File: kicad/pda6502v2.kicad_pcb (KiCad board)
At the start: 2 copper layers, 4 parts, among them U1 W65C02SxP, U2 AS6C62256-55PCN, U3 W65C22SxP, U4 AS6C62256-55PCN

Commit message: Lots of progress on schematic, some PCB part placement.
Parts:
- added C1: 0.1μF, Capacitor_SMD:C_0805_2012Metric_Pad1.18x1.45mm_HandSolder, B.Cu at (129.5, 91.4)
- added C10: 0.1μF, Capacitor_SMD:C_0805_2012Metric_Pad1.18x1.45mm_HandSolder, B.Cu at (119.4, 108.0)
- added C11: 0.1μF, Capacitor_SMD:C_0805_2012Metric_Pad1.18x1.45mm_HandSolder, B.Cu at (125.7, 133.9)
- added C12: 100uF, Capacitor_THT:CP_Radial_D5.0mm_P2.00mm, F.Cu at (106.7, 59.7)
- added C13: 10uF, Capacitor_THT:CP_Radial_D5.0mm_P2.00mm, F.Cu at (106.7, 67.7)
- added C14: 0.1μF, Capacitor_SMD:C_0805_2012Metric_Pad1.18x1.45mm_HandSolder, B.Cu at (125.7, 128.8)
- added C15: 0.1μF, Capacitor_SMD:C_0805_2012Metric_Pad1.18x1.45mm_HandSolder, B.Cu at (125.7, 123.7)
- added C16: 0.1μF, Capacitor_SMD:C_0805_2012Metric_Pad1.18x1.45mm_HandSolder, B.Cu at (125.7, 118.7)
- added C17: 0.1μF, Capacitor_SMD:C_0805_2012Metric_Pad1.18x1.45mm_HandSolder, B.Cu at (130.7, 133.9)
- added C18: 10nF, Capacitor_SMD:C_0805_2012Metric_Pad1.18x1.45mm_HandSolder, B.Cu at (119.4, 86.4)
- added C19: 10nF, Capacitor_SMD:C_0805_2012Metric_Pad1.18x1.45mm_HandSolder, B.Cu at (119.4, 82.5)
- added C2: 0.1μF, Capacitor_SMD:C_0805_2012Metric_Pad1.18x1.45mm_HandSolder, B.Cu at (170.2, 91.4)
- added C20: 10uF, Capacitor_SMD:C_0805_2012Metric_Pad1.18x1.45mm_HandSolder, B.Cu at (114.3, 86.4)
- added C21: 10uF, Capacitor_SMD:C_0805_2012Metric_Pad1.18x1.45mm_HandSolder, B.Cu at (114.3, 82.5)
- added C22: 0.1μF, Capacitor_SMD:C_0805_2012Metric_Pad1.18x1.45mm_HandSolder, B.Cu at (130.7, 128.8)
- added C23: 0.1μF, Capacitor_SMD:C_0805_2012Metric_Pad1.18x1.45mm_HandSolder, B.Cu at (130.7, 123.7)
- added C24: 0.1μF, Capacitor_SMD:C_0805_2012Metric_Pad1.18x1.45mm_HandSolder, B.Cu at (130.7, 118.7)
- added C3: 0.1μF, Capacitor_SMD:C_0805_2012Metric_Pad1.18x1.45mm_HandSolder, B.Cu at (169.9, 116.6)
- added C4: 0.1μF, Capacitor_SMD:C_0805_2012Metric_Pad1.18x1.45mm_HandSolder, B.Cu at (149.9, 124.5)
- added C5: 0.1μF, Capacitor_SMD:C_0805_2012Metric_Pad1.18x1.45mm_HandSolder, B.Cu at (185.4, 50.8)
- added C6: 0.1μF, Capacitor_SMD:C_0805_2012Metric_Pad1.18x1.45mm_HandSolder, B.Cu at (185.4, 71.1)
- added C7: 0.1μF, Capacitor_SMD:C_0805_2012Metric_Pad1.18x1.45mm_HandSolder, B.Cu at (185.4, 66.0)
- added C8: 0.1μF, Capacitor_SMD:C_0805_2012Metric_Pad1.18x1.45mm_HandSolder, B.Cu at (185.4, 86.4)
- added C9: 0.1μF, Capacitor_SMD:C_0805_2012Metric_Pad1.18x1.45mm_HandSolder, B.Cu at (149.9, 81.3)
- added D1: 1N5819, Diode_THT:D_DO-41_SOD81_P10.16mm_Horizontal, F.Cu at (120.7, 50.8)
- added D10: LED, LED_SMD:LED_0805_2012Metric_Pad1.15x1.40mm_HandSolder, F.Cu at (193.0, 92.2)
- added D2: LED, LED_THT:LED_D3.0mm, F.Cu at (106.7, 76.2)
- added D3: LED, LED_SMD:LED_0805_2012Metric_Pad1.15x1.40mm_HandSolder, F.Cu at (193.0, 109.9)
- added D4: LED, LED_SMD:LED_0805_2012Metric_Pad1.15x1.40mm_HandSolder, F.Cu at (193.0, 107.4)
- added D5: LED, LED_SMD:LED_0805_2012Metric_Pad1.15x1.40mm_HandSolder, F.Cu at (193.0, 104.9)
- added D6: LED, LED_SMD:LED_0805_2012Metric_Pad1.15x1.40mm_HandSolder, F.Cu at (193.0, 102.3)
- added D7: LED, LED_SMD:LED_0805_2012Metric_Pad1.15x1.40mm_HandSolder, F.Cu at (193.0, 99.8)
- added D8: LED, LED_SMD:LED_0805_2012Metric_Pad1.15x1.40mm_HandSolder, F.Cu at (193.0, 97.2)
- added D9: LED, LED_SMD:LED_0805_2012Metric_Pad1.15x1.40mm_HandSolder, F.Cu at (193.0, 94.7)
- added J1: GPIOA, Connector_PinHeader_2.54mm:PinHeader_2x07_P2.54mm_Vertical, F.Cu at (190.5, 50.8)
- added J2: GPIOB, Connector_PinHeader_2.54mm:PinHeader_2x07_P2.54mm_Vertical, F.Cu at (190.5, 71.1)
- added J3: UART, Connector_PinHeader_2.54mm:PinHeader_2x06_P2.54mm_Vertical, F.Cu at (190.5, 116.8)
- added J4: Screw_Terminal_01x02, TerminalBlock_Phoenix:TerminalBlock_Phoenix_MPT-0,5-2-2.54_1x02_P2.54mm_Horizontal, F.Cu at (104.1, 50.8)
- added J5: Conn_01x02, Connector_PinHeader_2.54mm:PinHeader_1x02_P2.54mm_Vertical, F.Cu at (111.8, 45.7)
- added J6: PMOD A, Connector_PinSocket_2.54mm:PinSocket_2x06_P2.54mm_Horizontal, F.Cu at (109.2, 116.8)
- added J7: PMOD B, Connector_PinSocket_2.54mm:PinSocket_2x06_P2.54mm_Horizontal, F.Cu at (109.2, 94.0)
- added JP1: Jumper, Connector_PinHeader_2.54mm:PinHeader_1x02_P2.54mm_Vertical, F.Cu at (119.4, 45.7)
- added R1: 10K, Resistor_SMD:R_0805_2012Metric_Pad1.20x1.40mm_HandSolder, B.Cu at (169.9, 121.7)
- added R10: 100Ω, Resistor_SMD:R_0805_2012Metric_Pad1.20x1.40mm_HandSolder, B.Cu at (115.2, 94.3)
- added R11: 100Ω, Resistor_SMD:R_0805_2012Metric_Pad1.20x1.40mm_HandSolder, B.Cu at (120.2, 96.8)
- added R12: 100Ω, Resistor_SMD:R_0805_2012Metric_Pad1.20x1.40mm_HandSolder, B.Cu at (115.2, 96.8)
- added R13: 100Ω, Resistor_SMD:R_0805_2012Metric_Pad1.20x1.40mm_HandSolder, B.Cu at (120.2, 120.3)
- added R14: 100Ω, Resistor_SMD:R_0805_2012Metric_Pad1.20x1.40mm_HandSolder, B.Cu at (115.2, 120.3)
- added R15: 100Ω, Resistor_SMD:R_0805_2012Metric_Pad1.20x1.40mm_HandSolder, B.Cu at (120.2, 117.8)
- added R16: 100Ω, Resistor_SMD:R_0805_2012Metric_Pad1.20x1.40mm_HandSolder, B.Cu at (115.2, 117.8)
- added R17: 100Ω, Resistor_SMD:R_0805_2012Metric_Pad1.20x1.40mm_HandSolder, B.Cu at (120.2, 101.9)
- added R18: 100Ω, Resistor_SMD:R_0805_2012Metric_Pad1.20x1.40mm_HandSolder, B.Cu at (115.2, 101.9)
- added R19: 100Ω, Resistor_SMD:R_0805_2012Metric_Pad1.20x1.40mm_HandSolder, B.Cu at (120.2, 104.5)
- added R2: 10K, Resistor_SMD:R_0805_2012Metric_Pad1.20x1.40mm_HandSolder, B.Cu at (175.0, 121.7)
- added R20: 100Ω, Resistor_SMD:R_0805_2012Metric_Pad1.20x1.40mm_HandSolder, B.Cu at (115.2, 104.5)
- added R21: 10K, Resistor_SMD:R_0805_2012Metric_Pad1.20x1.40mm_HandSolder, B.Cu at (102.9, 58.4)
- added R22: 10K, Resistor_SMD:R_0805_2012Metric_Pad1.20x1.40mm_HandSolder, B.Cu at (102.9, 62.2)
- added R23: 10K, Resistor_SMD:R_0805_2012Metric_Pad1.20x1.40mm_HandSolder, B.Cu at (128.2, 113.6)
- added R24: ?, Resistor_SMD:R_0805_2012Metric_Pad1.20x1.40mm_HandSolder, B.Cu at (102.9, 66.0)
- added R25: ?, Resistor_SMD:R_0805_2012Metric_Pad1.20x1.40mm_HandSolder, B.Cu at (102.9, 69.8)
- added R26: ?, Resistor_SMD:R_0805_2012Metric_Pad1.20x1.40mm_HandSolder, B.Cu at (102.9, 73.7)
- added R27: ?, Resistor_SMD:R_0805_2012Metric_Pad1.20x1.40mm_HandSolder, B.Cu at (102.9, 77.5)
- added R28: 1K, Resistor_SMD:R_0805_2012Metric_Pad1.20x1.40mm_HandSolder, B.Cu at (108.0, 72.4)
- added R29: 1K, Resistor_SMD:R_0805_2012Metric_Pad1.20x1.40mm_HandSolder, B.Cu at (187.9, 109.9)
- added R3: 10K, Resistor_SMD:R_0805_2012Metric_Pad1.20x1.40mm_HandSolder, B.Cu at (169.9, 124.2)
- added R30: 1K, Resistor_SMD:R_0805_2012Metric_Pad1.20x1.40mm_HandSolder, B.Cu at (187.9, 107.4)
- added R31: 1K, Resistor_SMD:R_0805_2012Metric_Pad1.20x1.40mm_HandSolder, B.Cu at (187.9, 104.9)
- added R32: 1K, Resistor_SMD:R_0805_2012Metric_Pad1.20x1.40mm_HandSolder, B.Cu at (187.9, 102.3)
- added R33: 1K, Resistor_SMD:R_0805_2012Metric_Pad1.20x1.40mm_HandSolder, B.Cu at (187.9, 99.8)
- added R34: 1K, Resistor_SMD:R_0805_2012Metric_Pad1.20x1.40mm_HandSolder, B.Cu at (187.9, 97.2)
- added R35: 1K, Resistor_SMD:R_0805_2012Metric_Pad1.20x1.40mm_HandSolder, B.Cu at (187.9, 94.7)
- added R36: 1K, Resistor_SMD:R_0805_2012Metric_Pad1.20x1.40mm_HandSolder, B.Cu at (187.9, 92.2)
- added R4: 10K, Resistor_SMD:R_0805_2012Metric_Pad1.20x1.40mm_HandSolder, B.Cu at (175.0, 124.2)
- added R5: 100Ω, Resistor_SMD:R_0805_2012Metric_Pad1.20x1.40mm_HandSolder, B.Cu at (120.2, 128.0)
- added R6: 100Ω, Resistor_SMD:R_0805_2012Metric_Pad1.20x1.40mm_HandSolder, B.Cu at (115.2, 128.0)
- added R7: 100Ω, Resistor_SMD:R_0805_2012Metric_Pad1.20x1.40mm_HandSolder, B.Cu at (120.2, 125.4)
- added R8: 100Ω, Resistor_SMD:R_0805_2012Metric_Pad1.20x1.40mm_HandSolder, B.Cu at (115.2, 125.4)
- added R9: 100Ω, Resistor_SMD:R_0805_2012Metric_Pad1.20x1.40mm_HandSolder, B.Cu at (120.2, 94.3)
- added REF**: MountingHole_3.2mm_M3, MountingHole:MountingHole_3.2mm_M3, F.Cu at (193.7, 136.3)
- added REF**: MountingHole_3.2mm_M3, MountingHole:MountingHole_3.2mm_M3, F.Cu at (101.7, 136.3)
- added REF**: MountingHole_3.2mm_M3, MountingHole:MountingHole_3.2mm_M3, F.Cu at (193.7, 44.3)
- added REF**: MountingHole_3.2mm_M3, MountingHole:MountingHole_3.2mm_M3, F.Cu at (101.7, 44.3)
- added SW1: SW_Push, Button_Switch_THT:SW_Tactile_Straight_KSA0Axx1LFTR, F.Cu at (101.6, 88.9)
- added U10: LT3030, Package_SO:HTSSOP-20-1EP_4.4x6.5mm_P0.65mm_EP2.85x4mm, F.Cu at (116.8, 83.8)
- added U5: AS6C4002-55PCN, Package_DIP:DIP-32_W15.24mm, F.Cu at (144.8, 88.9)
- added U6: AS6C4008-55PCN, Package_DIP:DIP-32_W15.24mm, F.Cu at (144.8, 45.7)
- added U7: AT25M01, Package_SO:SOIC-8_3.9x4.9mm_P1.27mm, F.Cu at (118.1, 102.9)
- added U8: ICE40HX4K-TQ144, Package_QFP:TQFP-144_20x20mm_P0.5mm, F.Cu at (127.0, 123.2)
- added U9: LM1117-3.3, Package_TO_SOT_THT:TO-220-3_Horizontal_TabDown, F.Cu at (114.3, 76.2)
- added X1: 3.6864 MHz, Oscillator:Oscillator_DIP-8, F.Cu at (168.9, 108.0)
- added X2: 10 MHz, Oscillator:Oscillator_DIP-8, F.Cu at (128.3, 106.7)
- U2: value AS6C62256-55PCN -> W65C22SxP; footprint Package_DIP:DIP-28_W15.24mm -> Package_DIP:DIP-40_W15.24mm
- U3: value W65C22SxP -> SC28L92A1B; footprint Package_DIP:DIP-40_W15.24mm -> Package_QFP:PQFP-44_10x10mm_P0.8mm
- U4: value AS6C62256-55PCN -> DS1818; footprint Package_DIP:DIP-28_W15.24mm -> Package_TO_SOT_SMD:SOT-23_Handsoldering
- moved U3 103.7 mm to (172.7, 120.4)
- moved U2 99.1 mm to (165.1, 45.7)
- moved U1 68.3 mm to (124.5, 45.7)
- moved U4 16.6 mm to (118.1, 94.0), turned to 180 degrees
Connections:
- U1 pad 1: Net-(U1-Pad1) -> /~VECPULL
- U1 pad 10: /ADDR1 -> /A1
- U1 pad 11: /ADDR2 -> /A2
- U1 pad 12: /ADDR3 -> /A3
- U1 pad 13: /ADDR4 -> /A4
- U1 pad 14: /ADDR5 -> /A5
- U1 pad 15: /ADDR6 -> /A6
- U1 pad 16: /ADDR7 -> /A7
- U1 pad 17: /ADDR8 -> /A8
- U1 pad 18: /ADDR9 -> /A9
- U1 pad 19: /ADDR10 -> /A10
- U1 pad 2: Net-(U1-Pad2) -> /READY
- U1 pad 20: /ADDR11 -> /A11
- U1 pad 22: /ADDR12 -> /A12
- U1 pad 23: /ADDR13 -> /A13
- U1 pad 24: /ADDR14 -> /A14
- U1 pad 25: /ADDR15 -> /A15
- U1 pad 26: /DATA7 -> /D7
- U1 pad 27: /DATA6 -> /D6
- U1 pad 28: /DATA5 -> /D5
- U1 pad 29: /DATA4 -> /D4
- U1 pad 30: /DATA3 -> /D3
- U1 pad 31: /DATA2 -> /D2
- U1 pad 32: /DATA1 -> /D1
- U1 pad 33: /DATA0 -> /D0
- U1 pad 34: Net-(U1-Pad34) -> /R~W
- U1 pad 36: Net-(U1-Pad36) -> /BUSEN
- U1 pad 37: /CLK -> /CLOCK
- U1 pad 38: Net-(U1-Pad38) -> /~SETOV
- U1 pad 4: Net-(U1-Pad4) -> /~IRQ
- U1 pad 40: /RESET -> /~RESET
- U1 pad 5: Net-(U1-Pad5) -> /~MLOCK
- U1 pad 6: Net-(U1-Pad6) -> /~NMIRQ
- U1 pad 7: Net-(U1-Pad7) -> /SYNC
- U1 pad 9: /ADDR0 -> /A0
- U2 pad 1: /ADDR14 -> GND
- U2 pad 10: /ADDR0 -> /PORTB_0
- U2 pad 11: /DATA0 -> /PORTB_1
- U2 pad 12: /DATA1 -> /PORTB_2
- U2 pad 13: /DATA2 -> /PORTB_3
- U2 pad 14: GND -> /PORTB_4
- U2 pad 15: /DATA3 -> /PORTB_5
- U2 pad 16: /DATA4 -> /PORTB_6
- U2 pad 17: /DATA5 -> /PORTB_7
- U2 pad 18: /DATA6 -> /PORTB_C1
- U2 pad 19: /DATA7 -> /PORTB_C2
- U2 pad 2: /ADDR12 -> /PORTA_0
- U2 pad 20: /RAM_LO_~CS -> +3V3
- U2 pad 21: /ADDR10 -> /VIA_~IRQ
- U2 pad 22: /RAM_LO_~CS -> /R~W
- U2 pad 23: /ADDR11 -> /VIA_~CS
- U2 pad 24: /ADDR9 -> +3V3
- U2 pad 25: /ADDR8 -> /CLOCK
- U2 pad 26: /ADDR13 -> /D7
- U2 pad 27: /RWB -> /D6
- U2 pad 28: +3V3 -> /D5
- U2 pad 3: /ADDR7 -> /PORTA_1
- U2 pad 4: /ADDR6 -> /PORTA_2
- U2 pad 5: /ADDR5 -> /PORTA_3
- U2 pad 6: /ADDR4 -> /PORTA_4
- U2 pad 7: /ADDR3 -> /PORTA_5
- U2 pad 8: /ADDR2 -> /PORTA_6
- U2 pad 9: /ADDR1 -> /PORTA_7
- U3 pad 1: GND -> /A3
- U3 pad 10: Net-(U3-Pad10) -> /UART_TXB~IRQ
- U3 pad 11: Net-(U3-Pad11) -> /UART_IM
- U3 pad 12: Net-(U3-Pad12) -> /D1
- U3 pad 13: Net-(U3-Pad13) -> /D3
- U3 pad 14: Net-(U3-Pad14) -> /D5
- U3 pad 15: Net-(U3-Pad15) -> /D7
- U3 pad 16: Net-(U3-Pad16) -> GND
- U3 pad 17: Net-(U3-Pad17) -> GND
- U3 pad 18: Net-(U3-Pad18) -> /UART_~IRQ
- U3 pad 19: Net-(U3-Pad19) -> /D6
- U3 pad 2: Net-(U3-Pad2) -> /UARTA_CTS
- U3 pad 20: +3V3 -> /D4
- U3 pad 21: Net-(U3-Pad21) -> /D2
- U3 pad 22: Net-(U3-Pad22) -> /D0
- U3 pad 24: Net-(U3-Pad24) -> /UART_TXA~IRQ
- U3 pad 25: /CLK -> /UART_RXA~IRQ
- U3 pad 26: /DATA7 -> Net-(U3-Pad26)
- U3 pad 27: /DATA6 -> /UARTA_RTS
- U3 pad 28: /DATA5 -> /UARTA_TX
- U3 pad 29: /DATA4 -> /UARTA_RX
- U3 pad 3: Net-(U3-Pad3) -> /UART_~WRN
- U3 pad 30: /DATA3 -> Net-(U3-Pad30)
- U3 pad 31: /DATA2 -> Net-(U3-Pad31)
- U3 pad 32: /DATA1 -> /RESET
- U3 pad 33: /DATA0 -> /UART_~CS
- U3 pad 35: /ADDR3 -> Net-(U3-Pad35)
- U3 pad 36: /ADDR2 -> Net-(U3-Pad36)
- U3 pad 37: /ADDR1 -> Net-(U3-Pad37)
- U3 pad 38: /ADDR0 -> +3V3
- U3 pad 39: Net-(U3-Pad39) -> +3V3
- U3 pad 4: Net-(U3-Pad4) -> /UART_~RDN
- U3 pad 40: Net-(U3-Pad40) -> /A0
- U3 pad 5: Net-(U3-Pad5) -> /UARTB_RX
- U3 pad 6: Net-(U3-Pad6) -> /UARTB_TX
- U3 pad 7: Net-(U3-Pad7) -> /UARTB_RTS
- U3 pad 9: Net-(U3-Pad9) -> /UART_RXB~IRQ
- U4 pad 1: /ADDR14 -> /~RESET
- U4 pad 2: /ADDR12 -> +3V3
- U4 pad 3: /ADDR7 -> GND
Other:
- board outline added: 100 x 100 mm
- copper layers 2 -> 4
- board text added: "pda6502v2"

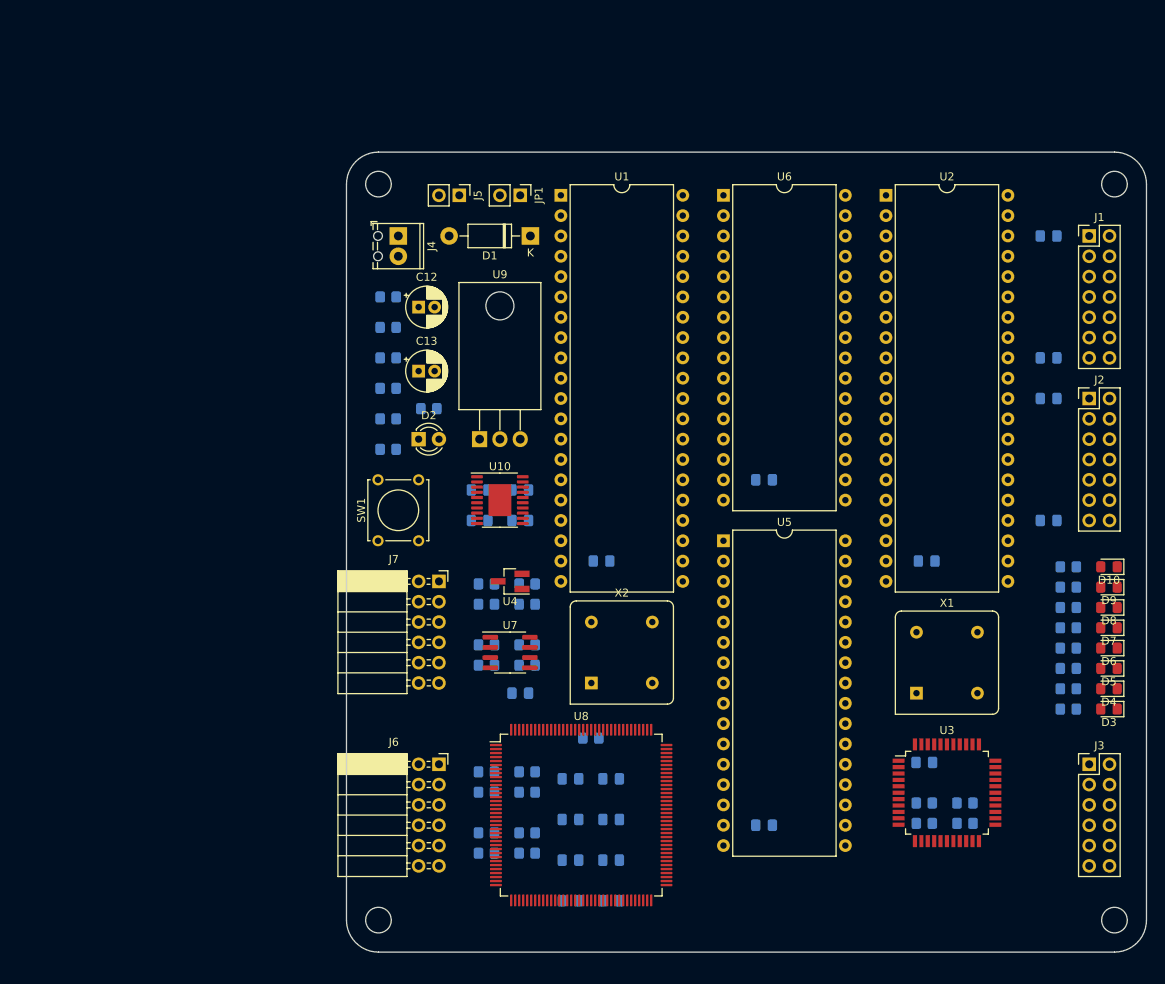
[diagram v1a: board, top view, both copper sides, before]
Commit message: WIP: remove PMOD. SMD LDO. Layout updates.
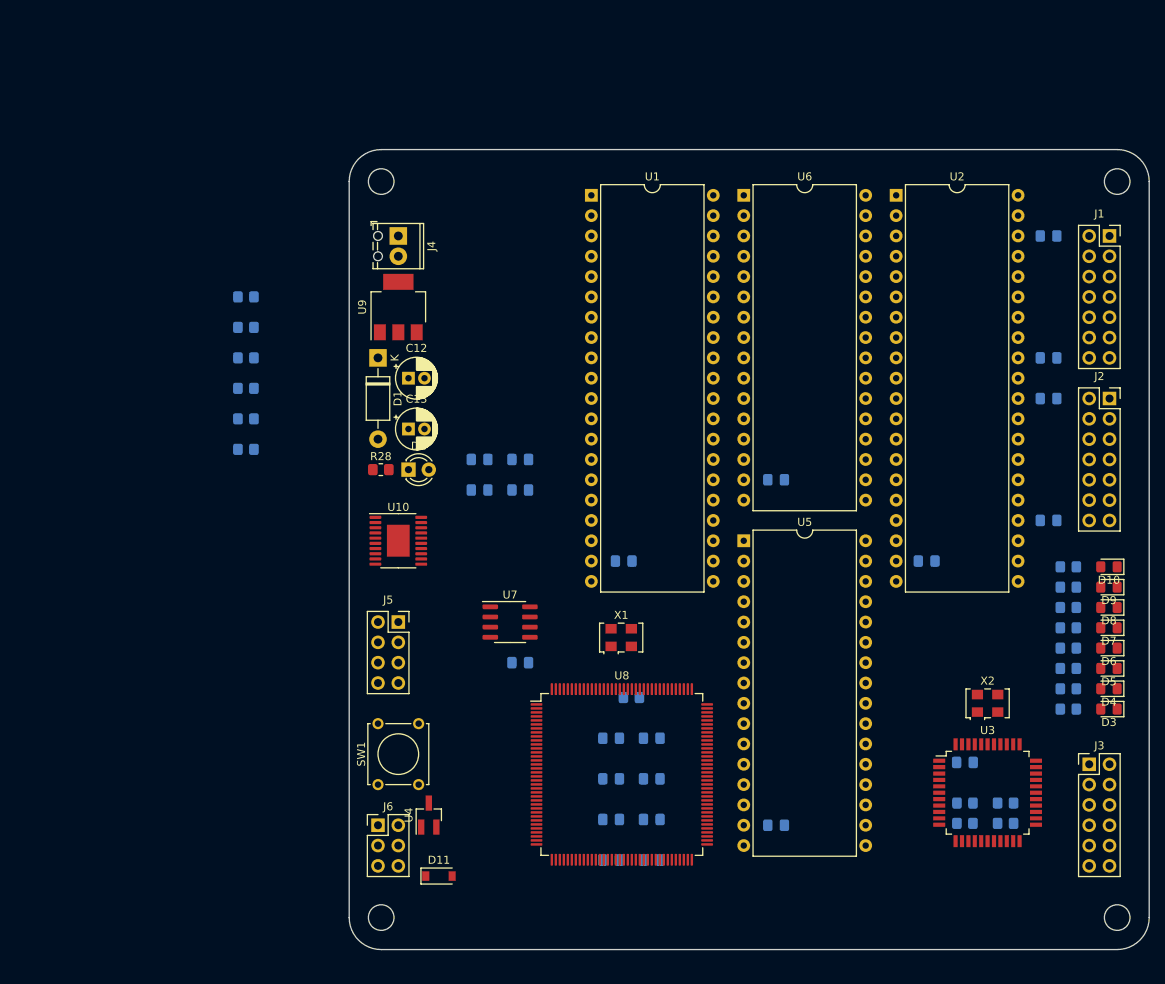
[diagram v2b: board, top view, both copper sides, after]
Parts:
- removed J7: PMOD B, Connector_PinSocket_2.54mm:PinSocket_2x06_P2.54mm_Horizontal
- removed JP1: Jumper, Connector_PinHeader_2.54mm:PinHeader_1x02_P2.54mm_Vertical
- removed R10, R11, R12, R13, R14, R15, R16, R17, R18, R19, R20, R5, R6, R7, R8, R9: 100Ω, Resistor_SMD:R_0805_2012Metric_Pad1.20x1.40mm_HandSolder
- removed the REF** at (193.7, 136.3)
- removed the REF** at (101.7, 136.3)
- removed the REF** at (193.7, 44.3)
- removed the REF** at (101.7, 44.3)
- added D11: 1N4148W, Diode_SMD:D_SOD-123, F.Cu at (109.2, 130.8)
- added REF**: MountingHole_3.2mm_M3, MountingHole:MountingHole_3.2mm_M3, F.Cu at (102.0, 136.0)
- added REF**: MountingHole_3.2mm_M3, MountingHole:MountingHole_3.2mm_M3, F.Cu at (102.0, 44.0)
- added REF**: MountingHole_3.2mm_M3, MountingHole:MountingHole_3.2mm_M3, F.Cu at (194.0, 136.0)
- added REF**: MountingHole_3.2mm_M3, MountingHole:MountingHole_3.2mm_M3, F.Cu at (194.0, 44.0)
- J1, J2: footprint Connector_PinHeader_2.54mm:PinHeader_2x07_P2.54mm_Vertical -> Connector_PinSocket_2.54mm:PinSocket_2x07_P2.54mm_Vertical
- J5: value Conn_01x02 -> Conn_02x04_Odd_Even; footprint Connector_PinHeader_2.54mm:PinHeader_1x02_P2.54mm_Vertical -> Connector_PinSocket_2.54mm:PinSocket_2x04_P2.54mm_Vertical
- J6: value PMOD A -> ICSP; footprint Connector_PinSocket_2.54mm:PinSocket_2x06_P2.54mm_Horizontal -> Connector_PinHeader_2.54mm:PinHeader_2x03_P2.54mm_Vertical
- R28: moved to F.Cu
- U5: value AS6C4002-55PCN -> AS6C4008-55PCN
- U9: value LM1117-3.3 -> TLV1117-33; footprint Package_TO_SOT_THT:TO-220-3_Horizontal_TabDown -> Package_TO_SOT_SMD:SOT-223
- X1: value 3.6864 MHz -> 10 MHz; footprint Oscillator:Oscillator_DIP-8 -> Oscillator:Oscillator_SMD_EuroQuartz_XO53-4Pin_5.0x3.2mm
- X2: value 10 MHz -> 3.6864 MHz; footprint Oscillator:Oscillator_DIP-8 -> Oscillator:Oscillator_SMD_EuroQuartz_XO53-4Pin_5.0x3.2mm
- moved J5 53.9 mm to (104.1, 99.1), turned to 0 degrees
- moved X2 49.6 mm to (177.8, 109.2)
- moved X1 37.6 mm to (132.0, 101.0)
- moved U4 30.9 mm to (108.0, 123.2), turned to 90 degrees
- moved SW1 30.5 mm to (101.6, 119.4)
- moved D1 24.4 mm to (101.6, 66.0), turned to 270 degrees
- moved U9 19.4 mm to (104.1, 59.7), turned to 90 degrees
- moved R21 17.8 mm to (85.1, 58.4)
- moved R22 17.8 mm to (85.1, 62.2)
- moved R24 17.8 mm to (85.1, 66.0)
- moved R25 17.8 mm to (85.1, 69.8)
- moved R26 17.8 mm to (85.1, 73.7)
- moved R27 17.8 mm to (85.1, 77.5)
- moved U10 13.7 mm to (104.1, 88.9)
- moved J6 10.8 mm to (101.6, 124.5)
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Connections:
- C10 pad 1: +3V3 -> Net-(C10-Pad1)
- J4 pad 1: Net-(J4-Pad1) -> Net-(D1-Pad2)
- J5 pad 1: Net-(J4-Pad1) -> GND
- J5 pad 2: GND -> +5V
- J6 pad 1: Net-(J6-Pad1) -> /FLASH_MISO
- J6 pad 2: Net-(J6-Pad2) -> Net-(C10-Pad1)
- J6 pad 3: Net-(J6-Pad3) -> /FLASH_SCK
- J6 pad 4: Net-(J6-Pad4) -> /FLASH_MOSI
- J6 pad 5: GND -> /FLASH_~CS
- J6 pad 6: +3V3 -> GND
- U7 pad 3: +3V3 -> Net-(C10-Pad1)
- U7 pad 7: +3V3 -> Net-(C10-Pad1)
- U7 pad 8: +3V3 -> Net-(C10-Pad1)
- U8 pad 1: /PMODA0 -> Net-(U8-Pad1)
- U8 pad 10: /PMODA7 -> Net-(U8-Pad10)
- U8 pad 11: /PMODB0 -> Net-(U8-Pad11)
- U8 pad 12: /PMODB1 -> Net-(U8-Pad12)
- U8 pad 15: /PMODB2 -> Net-(U8-Pad15)
- U8 pad 16: /PMODB3 -> Net-(U8-Pad16)
- U8 pad 17: /PMODB4 -> Net-(U8-Pad17)
- U8 pad 18: /PMODB5 -> Net-(U8-Pad18)
- U8 pad 19: /PMODB6 -> Net-(U8-Pad19)
- U8 pad 2: /PMODA1 -> Net-(U8-Pad2)
- U8 pad 20: /PMODB7 -> Net-(U8-Pad20)
- U8 pad 3: /PMODA2 -> Net-(U8-Pad3)
- U8 pad 4: /PMODA3 -> Net-(U8-Pad4)
- U8 pad 7: /PMODA4 -> Net-(U8-Pad7)
- U8 pad 8: /PMODA5 -> Net-(U8-Pad8)
- U8 pad 9: /PMODA6 -> Net-(U8-Pad9)
- X1 pad 4: GND -> +3V3
- X2 pad 4: GND -> +3V3

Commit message: Dual 6522 VIA; PCB layout progress.
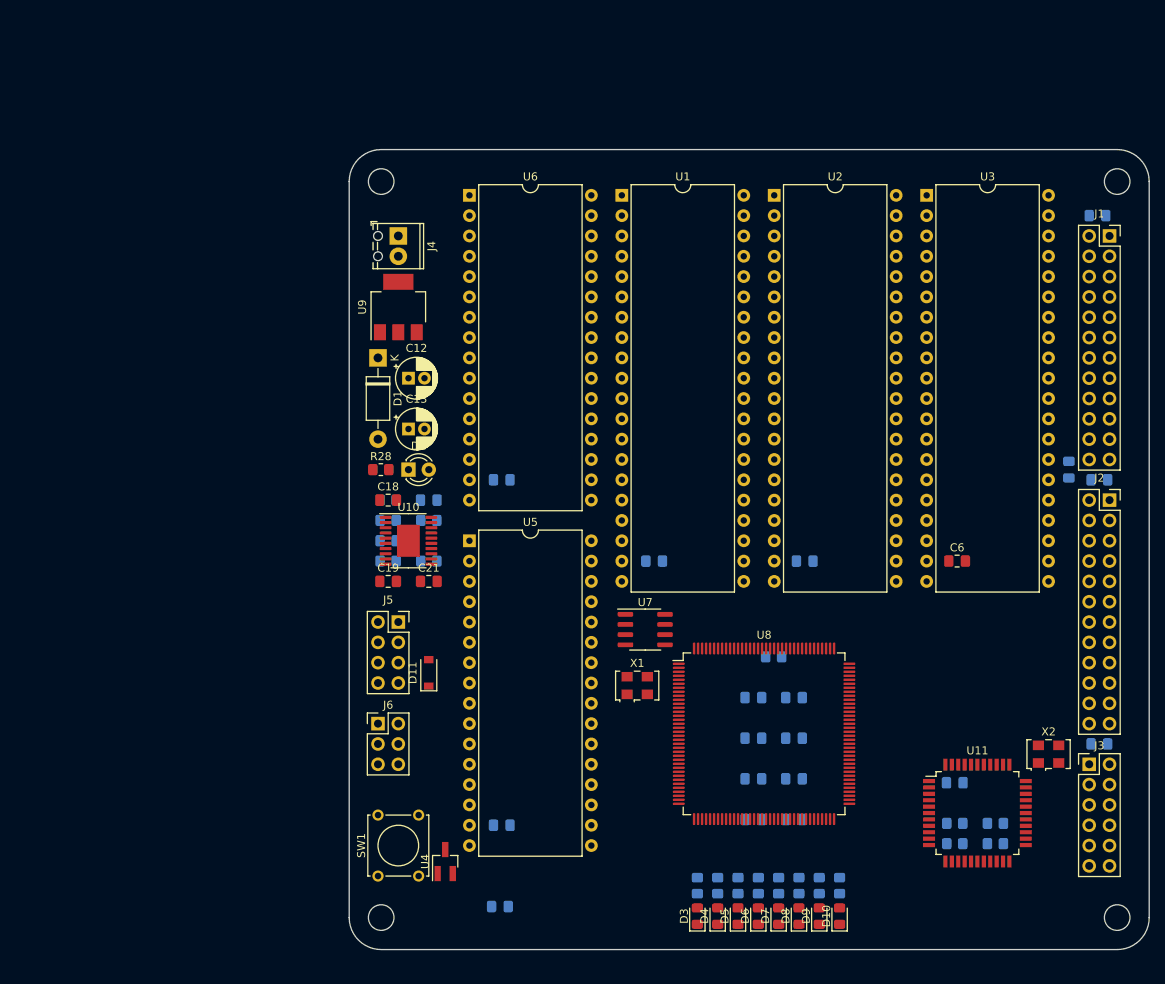
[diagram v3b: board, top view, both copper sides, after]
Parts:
- added C25: 0.1μF, Capacitor_SMD:C_0805_2012Metric_Pad1.18x1.45mm_HandSolder, B.Cu at (191.8, 114.3)
- added U3: W65C22SxP, Package_DIP:DIP-40_W15.24mm, F.Cu at (170.2, 45.7)
- C18, C19, C21, C6: moved to F.Cu
- J1: value GPIOA -> GPIO1; footprint Connector_PinSocket_2.54mm:PinSocket_2x07_P2.54mm_Vertical -> Connector_PinSocket_2.54mm:PinSocket_2x12_P2.54mm_Vertical
- J2: value GPIOB -> GPIO2; footprint Connector_PinSocket_2.54mm:PinSocket_2x07_P2.54mm_Vertical -> Connector_PinSocket_2.54mm:PinSocket_2x12_P2.54mm_Vertical
- X1: value 10 MHz -> 8 MHz
- moved D3 57.6 mm to (141.5, 135.8), turned to 90 degrees
- moved D4 56.6 mm to (144.1, 135.8), turned to 90 degrees
- moved D5 55.8 mm to (146.6, 135.8), turned to 90 degrees
- moved D6 55.2 mm to (149.1, 135.8), turned to 90 degrees
- moved D10 55.1 mm to (159.3, 135.8), turned to 90 degrees
- moved D7 54.8 mm to (151.7, 135.8), turned to 90 degrees
- moved D9 54.8 mm to (156.8, 135.8), turned to 90 degrees
- moved D8 54.7 mm to (154.2, 135.8), turned to 90 degrees
- moved R29 51.4 mm to (141.5, 132.0), turned to 90 degrees
- moved R30 50.3 mm to (144.1, 132.0), turned to 90 degrees
- moved R31 49.4 mm to (146.6, 132.0), turned to 90 degrees
- moved R36 49.0 mm to (159.3, 132.0), turned to 90 degrees
- moved R32 48.8 mm to (149.1, 132.0), turned to 90 degrees
- moved R35 48.6 mm to (156.8, 132.0), turned to 90 degrees
- moved R33 48.5 mm to (151.7, 132.0), turned to 90 degrees
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- renumbered U3 to U11
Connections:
- net /PORTA_0 renamed /GPIO1A0
- net /VIA_~CS renamed /VIA1_~CS
- net /VIA_~IRQ renamed /VIA1_~IRQ
- C6 pad 1: GND -> +3V3
- C6 pad 2: +3V3 -> GND
- C8 pad 1: GND -> +3V3
- C8 pad 2: +3V3 -> GND
- J1 pad 10: /PORTA_7 -> /GPIO1B3
- J1 pad 11: /PORTA_C1 -> /GPIO1A4
- J1 pad 12: /PORTA_C2 -> /GPIO1B4
- J1 pad 13: GND -> /GPIO1A5
- J1 pad 14: +3V3 -> /GPIO1B5
- J1 pad 4: /PORTA_1 -> /GPIO1B0
- J1 pad 5: /PORTA_2 -> /GPIO1A1
- J1 pad 6: /PORTA_3 -> /GPIO1B1
- J1 pad 7: /PORTA_4 -> /GPIO1A2
- J1 pad 8: /PORTA_5 -> /GPIO1B2
- J1 pad 9: /PORTA_6 -> /GPIO1A3
- J2 pad 10: /PORTB_7 -> /GPIO2B3
- J2 pad 11: /PORTB_C1 -> /GPIO2A4
- J2 pad 12: /PORTB_C2 -> /GPIO2B4
- J2 pad 13: GND -> /GPIO2A5
- J2 pad 14: +3V3 -> /GPIO2B5
- J2 pad 3: /PORTB_0 -> /GPIO2A0
- J2 pad 4: /PORTB_1 -> /GPIO2B0
- J2 pad 5: /PORTB_2 -> /GPIO2A1
- J2 pad 6: /PORTB_3 -> /GPIO2B1
- J2 pad 7: /PORTB_4 -> /GPIO2A2
- J2 pad 8: /PORTB_5 -> /GPIO2B2
- J2 pad 9: /PORTB_6 -> /GPIO2A3
- U2 pad 10: /PORTB_0 -> /GPIO1B0
- U2 pad 11: /PORTB_1 -> /GPIO1B1
- U2 pad 12: /PORTB_2 -> /GPIO1B2
- U2 pad 13: /PORTB_3 -> /GPIO1B3
- U2 pad 14: /PORTB_4 -> /GPIO1B4
- U2 pad 15: /PORTB_5 -> /GPIO1B5
- U2 pad 16: /PORTB_6 -> /GPIO1B6
- U2 pad 17: /PORTB_7 -> /GPIO1B7
- U2 pad 18: /PORTB_C1 -> /GPIO1BC1
- U2 pad 19: /PORTB_C2 -> /GPIO1BC2
- U2 pad 3: /PORTA_1 -> /GPIO1A1
- U2 pad 39: /PORTA_C2 -> /GPIO1AC2
- U2 pad 4: /PORTA_2 -> /GPIO1A2
- U2 pad 40: /PORTA_C1 -> /GPIO1AC1
- U2 pad 5: /PORTA_3 -> /GPIO1A3
- U2 pad 6: /PORTA_4 -> /GPIO1A4
- U2 pad 7: /PORTA_5 -> /GPIO1A5
- U2 pad 8: /PORTA_6 -> /GPIO1A6
- U2 pad 9: /PORTA_7 -> /GPIO1A7
- U8 pad 56: Net-(U8-Pad56) -> /VIA2_~IRQ
- U8 pad 60: Net-(U8-Pad60) -> /VIA2_~CS
